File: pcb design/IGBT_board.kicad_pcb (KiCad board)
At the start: 6 copper layers, 150 x 100 mm, 136 parts, among them Q1 IGBT, Q10 IGBT, Q11 IGBT, Q12 IGBT, Q13 NPN, Q14 PNP, Q15 CSD19533Q5A, Q16 CSD19533Q5A, Q17 NPN, Q18 PNP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

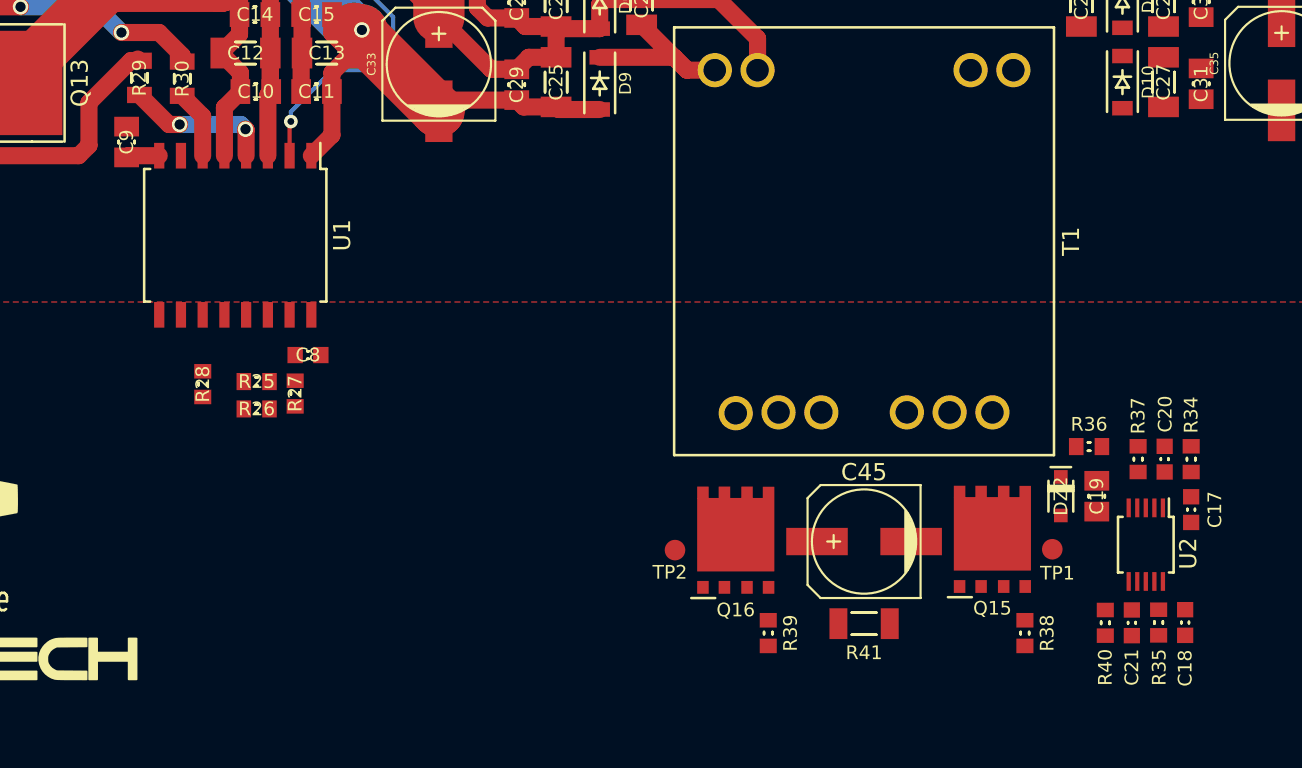
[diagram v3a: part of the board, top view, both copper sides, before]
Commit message: Larger gate resistors, added gate caps, added comments and images to the schematic
Signed-off-by: Marcos Chaparro <mchaparro@paltatech.com>
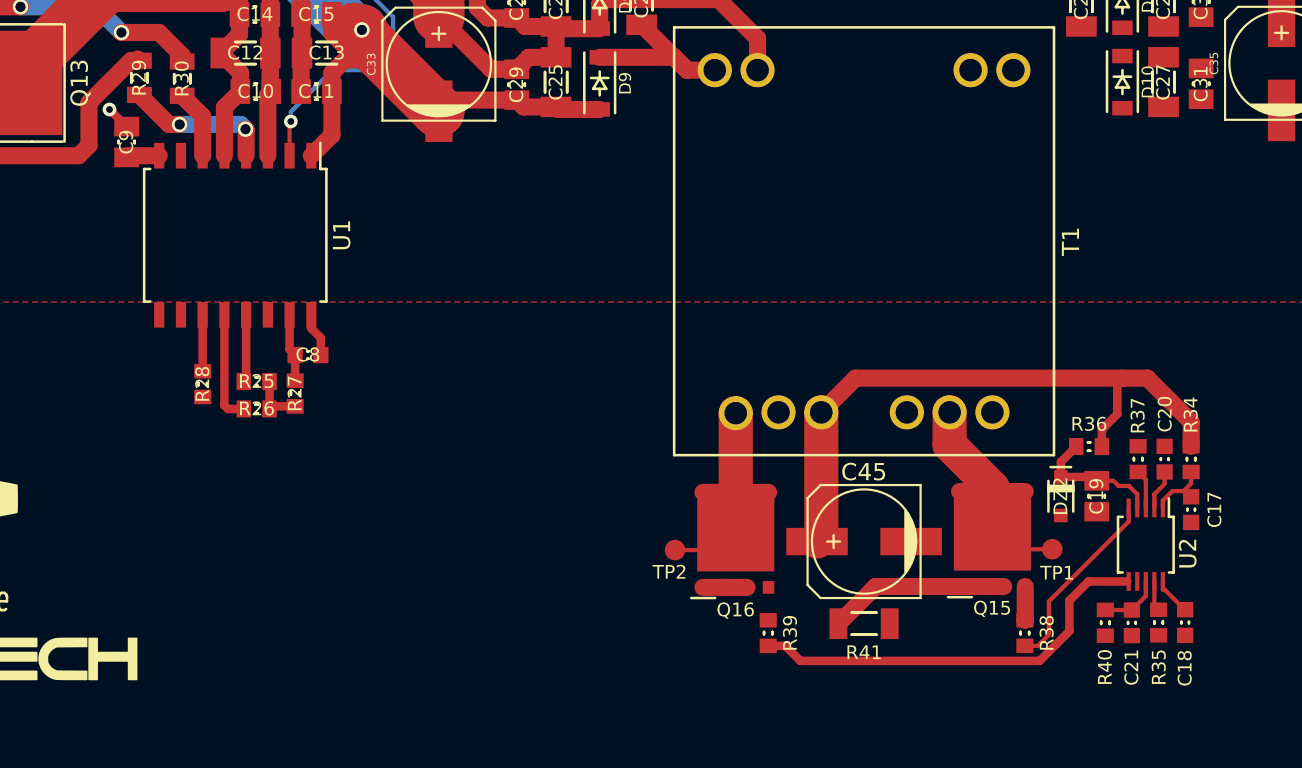
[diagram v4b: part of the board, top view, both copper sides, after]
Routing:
- net 24v: track 0.00 -> 37.1 mm
- net Net-(R39-Pad1): track 0.00 -> 24.3 mm
- net Net-(Q15-Pad5): track 0.00 -> 16.5 mm
- net Net-(Q16-Pad5): track 0.00 -> 16.2 mm
- net Net-(Q15-Pad1): track 0.00 -> 13.1 mm
- net Net-(R38-Pad2): track 0.00 -> 11.0 mm
- net Net-(C19-Pad1): track 0.00 -> 7.83 mm
- net /IGBT_driver_TOP/RDY: track 0.00 -> 6.51 mm
- net GND: track 0.00 -> 4.93 mm
- net Net-(C8-Pad1): track 0.00 -> 3.98 mm
- net /IGBT_driver_TOP/FAULT: track 0.00 -> 3.96 mm
- net /isolated power supply/CS: track 0.00 -> 3.55 mm
- net Net-(R28-Pad2): track 0.00 -> 3.30 mm
- net Net-(C17-Pad2): track 0.00 -> 3.16 mm
- net 3.3v: track 0.00 -> 3.16 mm
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
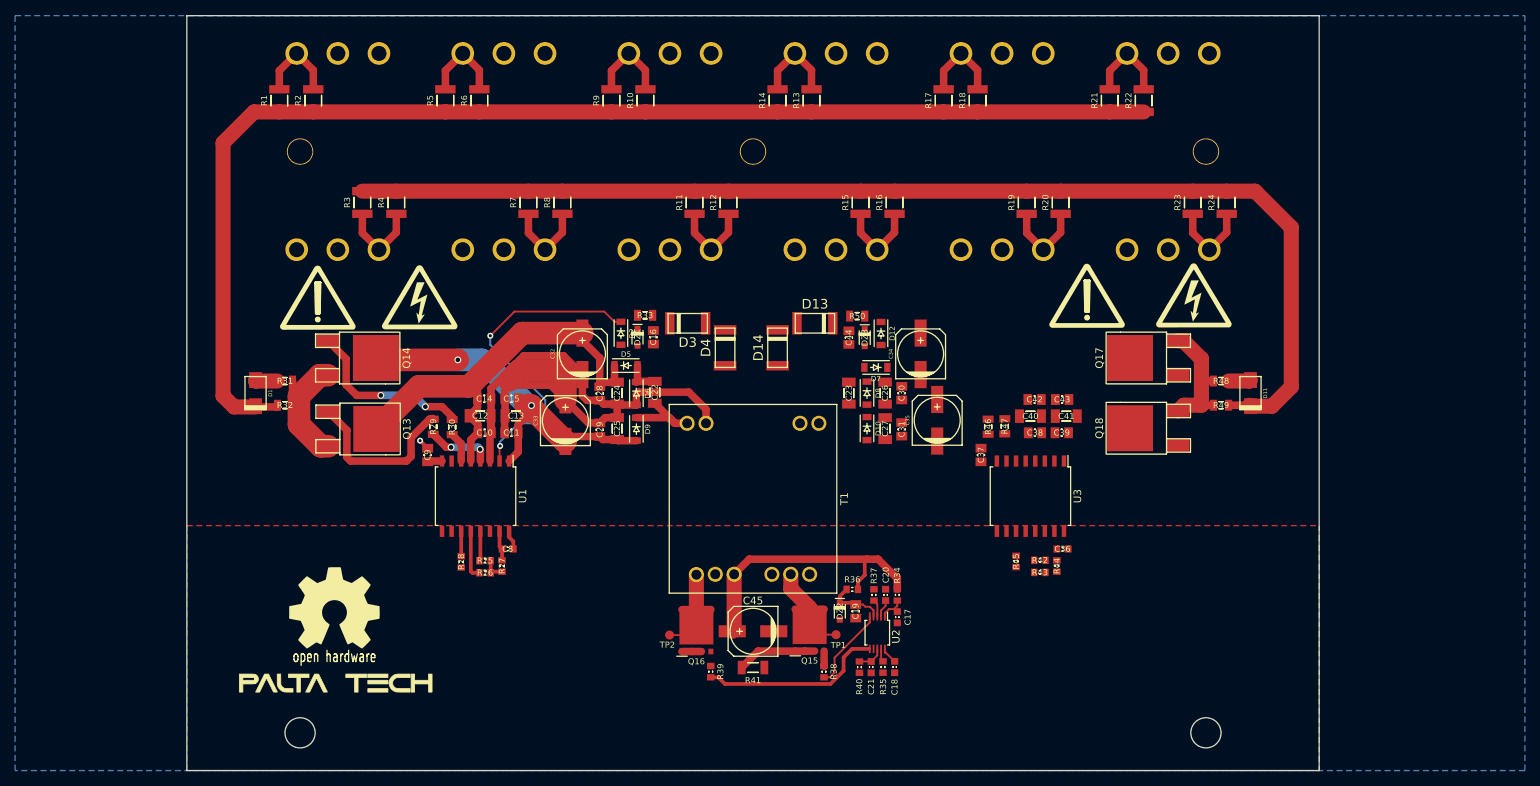
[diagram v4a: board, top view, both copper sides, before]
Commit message: Added 3D models, connector, more layout, updated readme
Signed-off-by: Marcos Chaparro <mchaparro@paltatech.com>
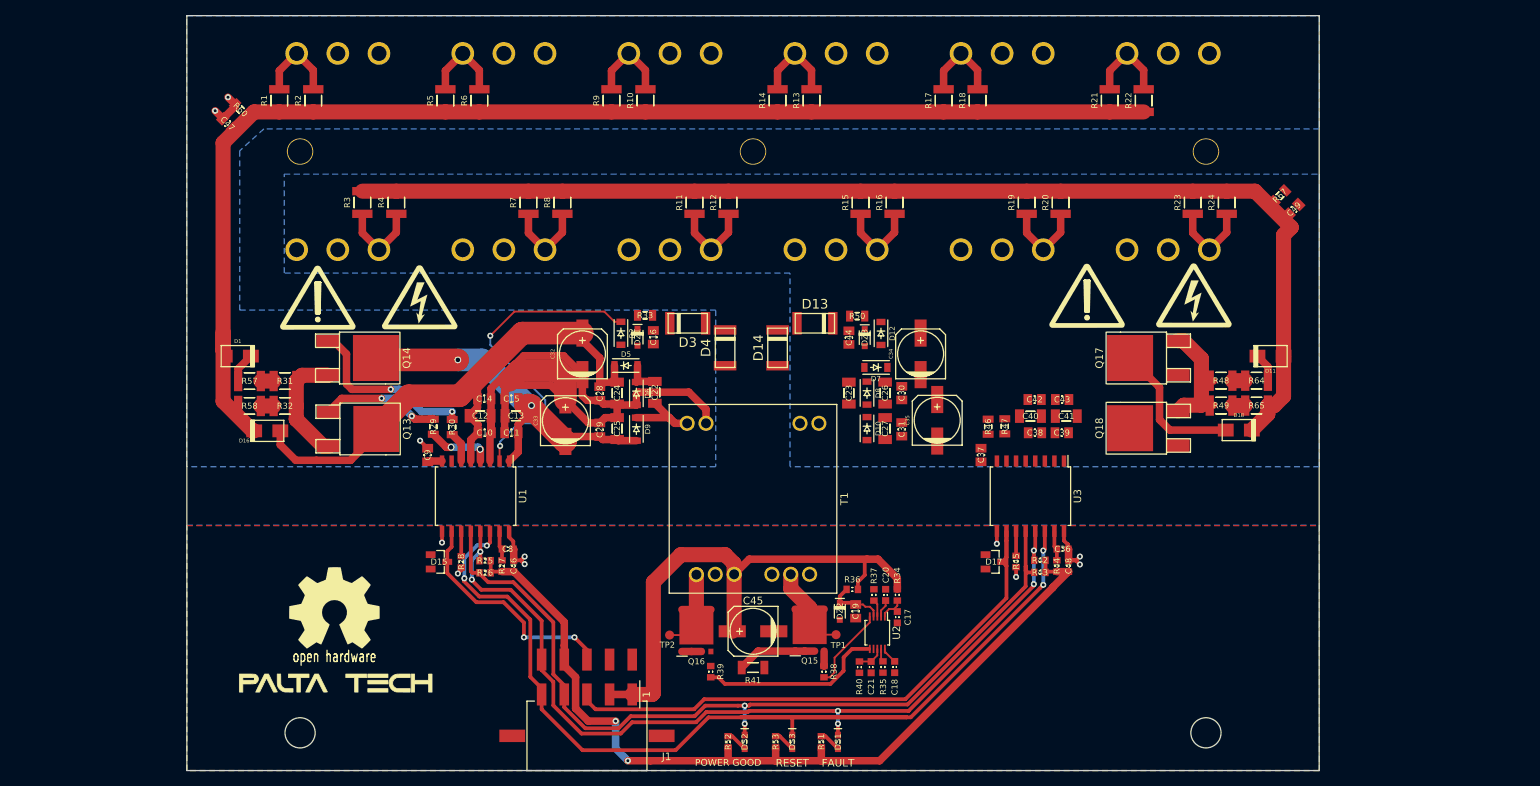
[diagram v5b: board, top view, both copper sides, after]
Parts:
- added C46: 10uF, IPC7351-Nominal:CAPC1608X55, F.Cu at (-31.7, 22.9)
- added C47: 5nF 50v, IPC7351-Nominal:CAPC2012X70, F.Cu at (-69.6, -35.7)
- added C48: 10uF, IPC7351-Nominal:CAPC1608X55, F.Cu at (41.8, 22.9)
- added C49: 5nF 50v, IPC7351-Nominal:CAPC2012X70, F.Cu at (71.7, -24.4)
- added D15: BAT54S, smd-semi:SOT-23, F.Cu at (-41.6, 22.4)
- added D16: SK310A-LTP, w_smd_diode:do214ac, F.Cu at (-64.3, 5.00)
- added D17: BAT54S, smd-semi:SOT-23, F.Cu at (31.9, 22.4)
- added D18: SK310A-LTP, w_smd_diode:do214ac, F.Cu at (64.3, 4.90)
- added DS1: FAULT, smd-semi:LED-0603, F.Cu at (11.2, 46.2)
- added DS2: PWR_GOOD, smd-semi:LED-0603, F.Cu at (-1.10, 46.2)
- added DS3: RESET, smd-semi:LED-0603, F.Cu at (5.20, 46.2)
- added J1: 4-794627-0, paltatech:TE-4-794627-0, F.Cu at (-22.0, 45.4)
- added R51: 1k, IPC7351-Nominal:RESC1608X50, F.Cu at (9.05, 46.2)
- added R52: 1k, IPC7351-Nominal:RESC1608X50, F.Cu at (-3.30, 46.2)
- added R53: 1k, IPC7351-Nominal:RESC1608X50, F.Cu at (3.00, 46.2)
- added R57: 1R, IPC7351-Nominal:RESC3225X60, F.Cu at (-66.7, -1.60)
- added R58: 2R, IPC7351-Nominal:RESC3225X60, F.Cu at (-66.7, 1.70)
- added R60: 4.7k, IPC7351-Nominal:RESC2012X50, F.Cu at (-67.9, -37.5)
- added R64: 1R, IPC7351-Nominal:RESC3225X60, F.Cu at (66.7, -1.65)
- added R65: 2R, IPC7351-Nominal:RESC3225X60, F.Cu at (66.7, 1.65)
- added R67: 4.7k, IPC7351-Nominal:RESC2012X50, F.Cu at (69.8, -26.1)
- R29, R30, R46, R47: value R-0805 -> 10R
- R31, R48: value 10R -> 1R; footprint IPC7351-Nominal:RESC2012X50 -> IPC7351-Nominal:RESC3225X60
- R32, R49: value 0R -> 2R; footprint IPC7351-Nominal:RESC2012X50 -> IPC7351-Nominal:RESC3225X60
- U2: footprint TSSOP-10_3x3mm_Pitch0.5mm -> Housings_SSOP:TSSOP-10_3x3mm_Pitch0.5mm
- moved D11 5.57 mm to (68.5, -4.90), turned to 180 degrees
- moved D1 5.43 mm to (-68.2, -4.90), turned to 0 degrees
- moved R32 0.10 mm to (-62.0, 1.70)
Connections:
- D1 pad 1: Net-(D1-Pad1) -> GATE_HIGH
- D1 pad 2: GATE_HIGH -> Net-(D1-Pad2)
- D11 pad 1: Net-(D11-Pad1) -> GATE_LOW
- D11 pad 2: GATE_LOW -> Net-(D11-Pad2)
- R25 pad 2: /IGBT_driver_TOP/FAULT -> /FAULT
- R26 pad 2: /IGBT_driver_TOP/RDY -> /READY
- R31 pad 1: Net-(D1-Pad1) -> Net-(R31-Pad1)
- R32 pad 1: GATE_HIGH -> Net-(R32-Pad1)
- R42 pad 2: /IGBT_driver_BOT/FAULT -> /FAULT
- R43 pad 2: /IGBT_driver_BOT/RDY -> /READY
- R48 pad 1: Net-(D11-Pad1) -> Net-(R48-Pad1)
- R49 pad 1: GATE_LOW -> Net-(R49-Pad1)
- U1 pad 10: /IGBT_driver_TOP/IN+ -> /IN_TOP
- U1 pad 12: /IGBT_driver_TOP/RDY -> /READY
- U1 pad 13: /IGBT_driver_TOP/FAULT -> /FAULT
- U1 pad 14: /IGBT_driver_TOP/RESET -> /RESET
- U3 pad 10: /IGBT_driver_BOT/IN+ -> /IN_BOTTOM
- U3 pad 12: /IGBT_driver_BOT/RDY -> /READY
- U3 pad 13: /IGBT_driver_BOT/FAULT -> /FAULT
- U3 pad 14: /IGBT_driver_BOT/RESET -> /RESET
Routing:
- net /RESET: track 0.00 -> 141.2 mm, vias 0 -> 4
- net /FAULT: track 0.00 -> 116.7 mm, vias 0 -> 6
- net /READY: track 0.00 -> 114.1 mm, vias 0 -> 2
- net 3.3v: track 3.16 -> 117.0 mm, vias 0 -> 2
- net /IN_BOTTOM: track 0.00 -> 76.9 mm
- net 24v: track 37.1 -> 71.8 mm
- net /IN_TOP: track 0.00 -> 30.9 mm, vias 0 -> 2
- net /IGBT_driver_BOT/+15V: track 0.00 -> 19.1 mm
- net /IGBT_driver_TOP/+15V: track 61.8 -> 79.5 mm
- net GND: track 4.93 -> 21.8 mm, vias 0 -> 8
- net GATE_HIGH: track 165.0 -> 173.5 mm
- net /IGBT_driver_TOP/RDY: track 6.51 -> 0.00 mm
- net Net-(Q13-Pad1): track 22.8 -> 16.6 mm, vias 0 -> 2
- net PHASE: track 88.6 -> 94.0 mm, vias 1 -> 3
- net Net-(D1-Pad2): track 0.00 -> 4.00 mm
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- added copper zone on B.Cu, net GND
- added copper zone on B.Cu, net VBUS-
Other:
- board text added: "FAULT"
- board text added: "POWER GOOD"
- board text added: "RESET"

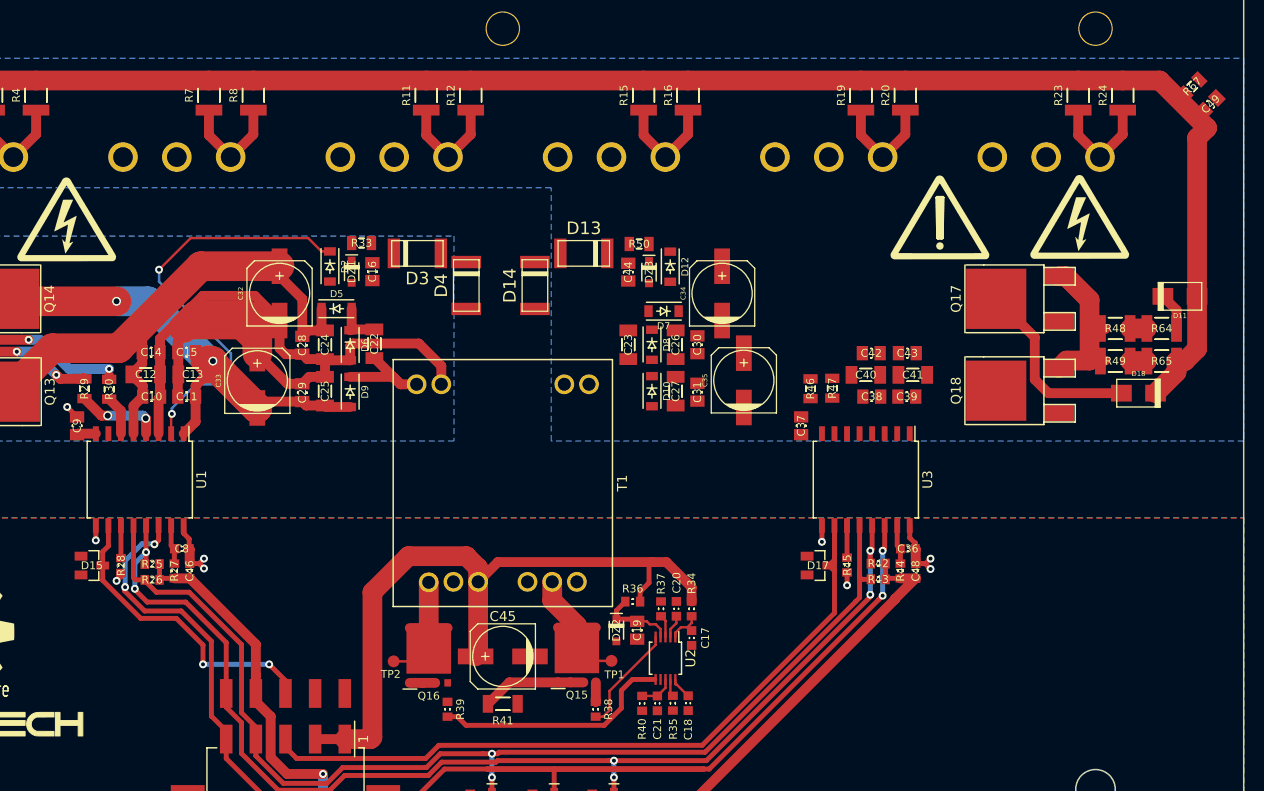
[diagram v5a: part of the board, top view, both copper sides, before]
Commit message: Added testpoints
Signed-off-by: Marcos Chaparro <mchaparro@paltatech.com>
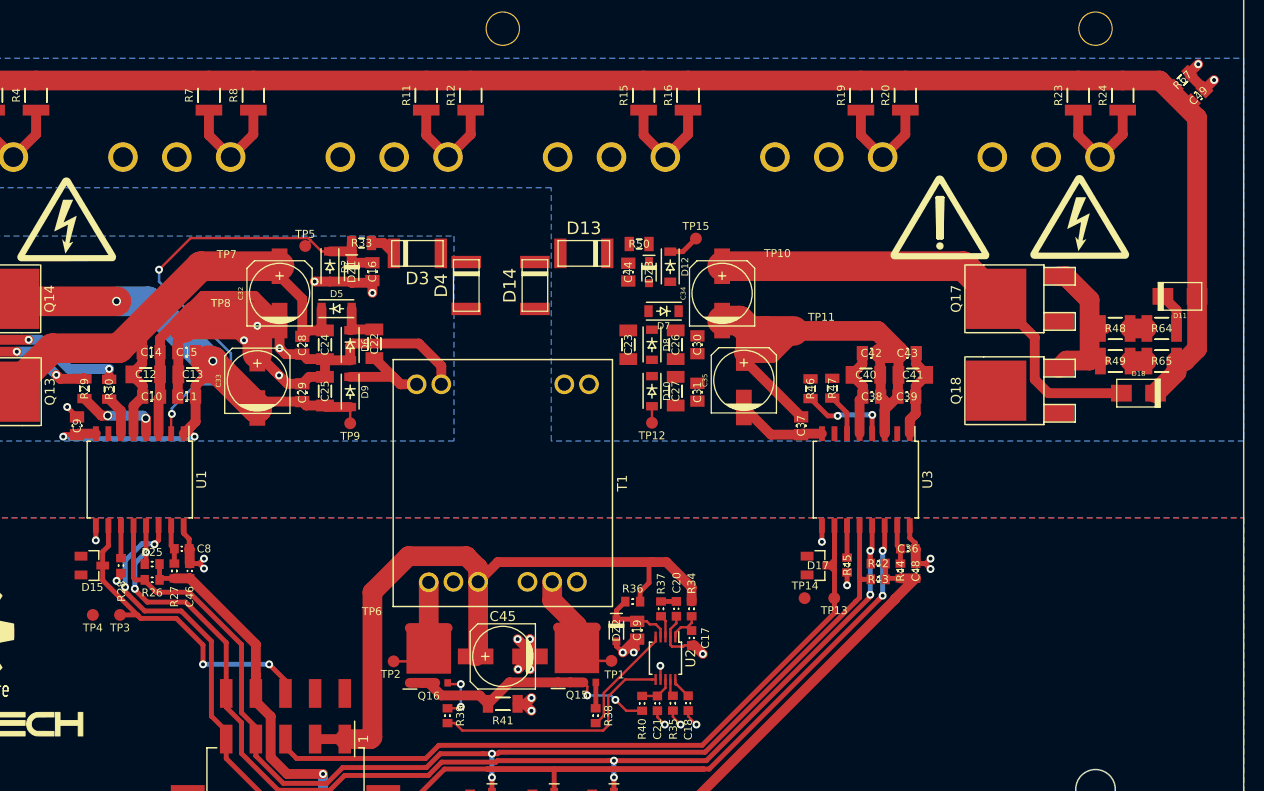
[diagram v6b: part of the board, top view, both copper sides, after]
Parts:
- added TP10: 15v, conn-test:TEST-SMD-SMALL, F.Cu at (27.8, -7.95)
- added TP11: GND, conn-test:TEST-SMD-SMALL, F.Cu at (32.2, -1.40)
- added TP12: -8v, conn-test:TEST-SMD-SMALL, F.Cu at (15.1, 7.90)
- added TP13: IN, conn-test:TEST-SMD-SMALL, F.Cu at (33.5, 25.6)
- added TP14: GND, conn-test:TEST-SMD-SMALL, F.Cu at (30.6, 25.6)
- added TP15: DESAT, conn-test:TEST-SMD-SMALL, F.Cu at (19.6, -10.8)
- added TP3: IN, conn-test:TEST-SMD-SMALL, F.Cu at (-38.8, 27.4)
- added TP4: GND, conn-test:TEST-SMD-SMALL, F.Cu at (-41.5, 27.4)
- added TP5: DESAT, conn-test:TEST-SMD-SMALL, F.Cu at (-20.0, -10.0)
- added TP6: 24v, conn-test:TEST-SMD-SMALL, F.Cu at (-13.2, 28.2)
- added TP7: 15v, conn-test:TEST-SMD-SMALL, F.Cu at (-27.9, -7.95)
- added TP8: GND, conn-test:TEST-SMD-SMALL, F.Cu at (-28.6, -3.00)
- added TP9: -8v, conn-test:TEST-SMD-SMALL, F.Cu at (-15.4, 7.95)
- TP1: value TESTPOINT -> SW1
- TP2: value TESTPOINT -> SW2
- moved C49 1.51 mm to (70.4, -25.2)
- moved R67 1.19 mm to (68.8, -26.8)
- moved R38 0.65 mm to (9.40, 37.5)
- moved R39 0.65 mm to (-5.60, 37.5)
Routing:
- net VBUS-: track 0.00 -> 63.6 mm, vias 0 -> 2
- net /IGBT_driver_BOT/+15V: track 19.1 -> 63.1 mm
- net GND: track 21.8 -> 48.3 mm, vias 8 -> 21
- net /IGBT_driver_BOT/-8V: track 0.00 -> 20.1 mm
- net /IGBT_driver_TOP/-8V: track 61.3 -> 79.1 mm, vias 2 -> 4
- net Net-(Q15-Pad1): track 13.1 -> 27.7 mm, vias 0 -> 2
- net PHASE: track 94.0 -> 103.7 mm, vias 3 -> 9
- net Net-(R46-Pad2): track 0.00 -> 8.92 mm, vias 0 -> 2
- net Net-(C16-Pad1): track 42.7 -> 49.7 mm
- net Net-(Q16-Pad4): track 0.00 -> 5.10 mm, vias 0 -> 2
- net Net-(R47-Pad2): track 0.00 -> 4.22 mm
- net Net-(C44-Pad1): track 0.00 -> 3.15 mm
- net Net-(D3-Pad2): track 0.00 -> 2.71 mm
- net /IN_TOP: track 30.9 -> 32.8 mm
- net Net-(C20-Pad1): track 0.00 -> 1.55 mm
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- added copper zone on Ext1(PHASE).Cu, net PHASE
- added copper zone on Ext2(VBUS+).Cu, net VBUS+
- added copper zone on Ext3(VBUS-).Cu, net VBUS-
- removed copper zone on In2.Cu, net PHASE
